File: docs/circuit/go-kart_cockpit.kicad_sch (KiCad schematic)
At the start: 28 parts, among them P1 Power, Q1 TIP120, SW1 SW_MEC_5E, X1 AVR-ISP-10, X10 Bluetooth-Modul, X11 Start/Stop/Rückwärts, X12 Taster rechts (male), X13 Taster links (male), X2 Display (2x3 male), X3 5V, X4 GND, X5 SDA, X6 24V Hupe, X7 J5, X8 J3, X9 SCL

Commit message: feat: first sketch of PCB
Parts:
- removed JP1: ~, Library:Bridge, symbol Jumper:Jumper_2_Bridged
- added JP10: Display_Vcc, Resistor_THT:R_Axial_DIN0207_L6.3mm_D2.5mm_P7.62mm_Horizontal, symbol Jumper:Jumper_2_Bridged
- added JP11: GND, Resistor_THT:R_Axial_DIN0207_L6.3mm_D2.5mm_P7.62mm_Horizontal, symbol Jumper:Jumper_2_Bridged
- added JP12: Display_Vcc, Resistor_THT:R_Axial_DIN0207_L6.3mm_D2.5mm_P15.24mm_Horizontal, symbol Jumper:Jumper_2_Bridged
- added JP2: GND, Resistor_THT:R_Axial_DIN0207_L6.3mm_D2.5mm_P15.24mm_Horizontal, symbol Jumper:Jumper_2_Bridged
- added JP3: ISP_SCK, Resistor_THT:R_Axial_DIN0207_L6.3mm_D2.5mm_P10.16mm_Horizontal, symbol Jumper:Jumper_2_Bridged
- added JP4: ISP_MOSI, Resistor_THT:R_Axial_DIN0207_L6.3mm_D2.5mm_P15.24mm_Horizontal, symbol Jumper:Jumper_2_Bridged
- added JP5: TXD0, Resistor_THT:R_Axial_DIN0207_L6.3mm_D2.5mm_P10.16mm_Horizontal, symbol Jumper:Jumper_2_Bridged
- added JP6: RXD0, Resistor_THT:R_Axial_DIN0207_L6.3mm_D2.5mm_P10.16mm_Horizontal, symbol Jumper:Jumper_2_Bridged
- added JP8: GND, Resistor_THT:R_Axial_DIN0207_L6.3mm_D2.5mm_P10.16mm_Horizontal, symbol Jumper:Jumper_2_Bridged
- added JP9: ~, Resistor_THT:R_Axial_DIN0207_L6.3mm_D2.5mm_P15.24mm_Horizontal, symbol Jumper:Jumper_2_Bridged
- P1: footprint LED_THT:LED_D5.0mm_Horizontal_O3.81mm_Z15.0mm -> LED_THT:LED_D3.0mm_Horizontal_O1.27mm_Z6.0mm
- Q1: footprint Package_TO_SOT_THT:TO-220-3_Horizontal_TabDown -> Library:TO-220-3_Horizontal_TabDown_no_hole
- R4: footprint Resistor_THT:R_Axial_DIN0204_L3.6mm_D1.6mm_P7.62mm_Horizontal -> Resistor_THT:R_Axial_DIN0309_L9.0mm_D3.2mm_P25.40mm_Horizontal
- R5: footprint Resistor_THT:R_Axial_DIN0204_L3.6mm_D1.6mm_P7.62mm_Horizontal -> Resistor_THT:R_Axial_DIN0207_L6.3mm_D2.5mm_P15.24mm_Horizontal
- R6: footprint Resistor_THT:R_Axial_DIN0204_L3.6mm_D1.6mm_P7.62mm_Horizontal -> Resistor_THT:R_Axial_DIN0207_L6.3mm_D2.5mm_P10.16mm_Horizontal
- X10: footprint Connector_JST:JST_EH_S4B-EH_1x04_P2.50mm_Horizontal -> Connector_PinSocket_2.54mm:PinSocket_1x04_P2.54mm_Horizontal
- X11, X6: footprint Library:Elecbee_3pin_Green_Connector_1.5mm -> Connector_Phoenix_MC_HighVoltage:PhoenixContact_MC_1,5_3-G-5.08_1x03_P5.08mm_Horizontal
- X2: value Display (2x3 male) -> Display (male)
- X3, X4, X5, X9: footprint Connector_PinHeader_2.54mm:PinHeader_1x01_P2.54mm_Vertical -> Connector_PinSocket_2.54mm:PinSocket_1x01_P2.54mm_Vertical
- X7, X8: footprint Connector_PinHeader_2.54mm:PinHeader_2x13_P2.54mm_Vertical -> Connector_PinSocket_2.54mm:PinSocket_2x13_P2.54mm_Vertical
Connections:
- net +24V: now also X6.3 (Pin_3); no longer X6.2 (Pin_2)
- net GND: now also X10.3 (Pin_3), JP11.1 (A), JP11.2 (B), JP2.1 (A), JP2.2 (B), JP8.1 (A), JP8.2 (B); no longer X10.2 (Pin_2)
- net PB1_SCK: now also X8.17 (Pin_17), JP3.1 (A); no longer X1.7 (SCK), X8.18 (Pin_18)
- net PB2_MOSI: now also X8.16 (Pin_16), JP4.1 (A); no longer X1.1 (MOSI), X8.15 (Pin_15)
- net PB3_MISO: now also X8.15 (Pin_15); no longer X8.16 (Pin_16)
- net PB4_OC2A: now also X8.14 (Pin_14); no longer X8.13 (Pin_13)
- net PC0_SW_BlinkerR: now also X7.24 (Pin_24); no longer X7.23 (Pin_23)
- net PC3_LED_BlinkerR: now also X7.26 (Pin_26); no longer X7.25 (Pin_25)
- net PD0_SCL: now also X7.14 (Pin_14); no longer X7.13 (Pin_13)
- net PD1_SDA: now also X7.13 (Pin_13); no longer X7.14 (Pin_14)
- net PD2_RXD1: now also X10.2 (Pin_2), X7.16 (Pin_16), JP9.1 (A), JP9.2 (B); no longer X10.3 (Pin_3)
- net PD3_TXD1: now also X7.15 (Pin_15); no longer X7.16 (Pin_16)
- net PD4_LED_GearUp: now also X7.18 (Pin_18); no longer X7.17 (Pin_17)
- net PE0_RXD0: now also X8.26 (Pin_26), JP6.1 (A); no longer X2.6 (Pin_6), X8.25 (Pin_25)
- net PE1_TXD0: now also X8.25 (Pin_25), JP5.1 (A); no longer X2.2 (Pin_2), X8.26 (Pin_26)
- net PE2_LED_BlinkerL: now also X8.24 (Pin_24); no longer X8.23 (Pin_23)
- net PE3_SW_BlinkerL: now also X8.23 (Pin_23); no longer X8.24 (Pin_24)
- net PE4_LED_LightSwitch: now also X8.22 (Pin_22); no longer X8.21 (Pin_21)
- net PE5_SW_LightSwitch: now also X8.21 (Pin_21); no longer X8.22 (Pin_22)
- net PE6_LED_Warnblinker: now also X8.20 (Pin_20); no longer X8.19 (Pin_19)
- net PE7_SW_Warnblinker: now also X8.19 (Pin_19); no longer X8.20 (Pin_20)
- net PG0_SW_GearUp: now also X7.20 (Pin_20); no longer X7.19 (Pin_19)
- net PG2_SW_GearDown: now also X7.22 (Pin_22); no longer X7.21 (Pin_21)
- net PG3_LED_GearDown: now also X7.12 (Pin_12); no longer X7.11 (Pin_11)
- net Vcc (5V): now also X10.4 (Pin_4), JP10.1 (A), JP10.2 (B), JP12.1 (A), JP12.2 (B); no longer X10.1 (Pin_1)
- net /PC2_SW_Start: now also X7.23 (Pin_23); no longer X7.24 (Pin_24)
- net /PG1_SW_Reverse: now also X7.19 (Pin_19); no longer X7.20 (Pin_20)
- net /RESET: now also X7.25 (Pin_25); no longer X7.26 (Pin_26)
- net at R5.2, R6.1: now also X10.1 (Pin_1); no longer X10.4 (Pin_4)
- net at Q1.2 (C), R3.2 (A): now also X6.2 (Pin_2); no longer X6.3 (Pin_3)
- net at R7.2: now also X11.1; no longer X11.3 (4)
- net at R8.2: now also X11.3 (4); no longer X11.1
- new net: JP5.2 (B), X2.2 (Pin_2)
- new net: JP6.2 (B), X2.6 (Pin_6)
- new net: JP4.2 (B), X1.1 (MOSI)
- new net: JP3.2 (B), X1.7 (SCK)
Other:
- moved on the sheet: R1, R7, R8, X1, X2, X5, X6, X7, X8, X9

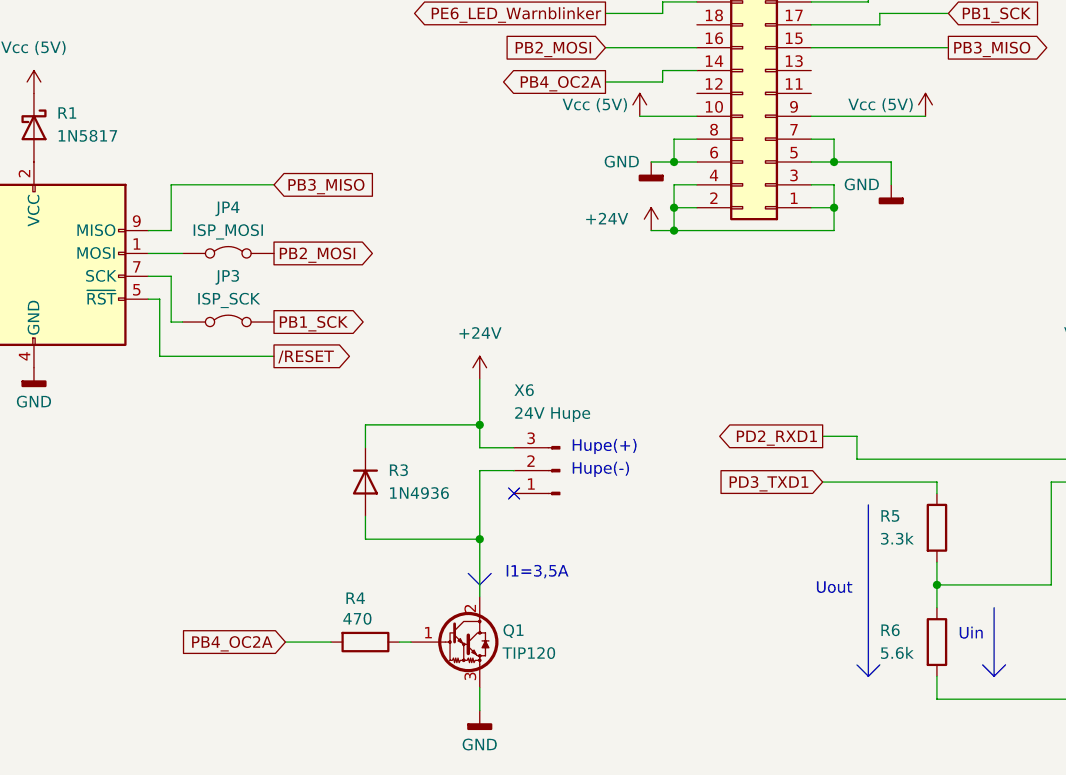
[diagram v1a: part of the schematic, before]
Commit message: feat(circuit): fixed DRC
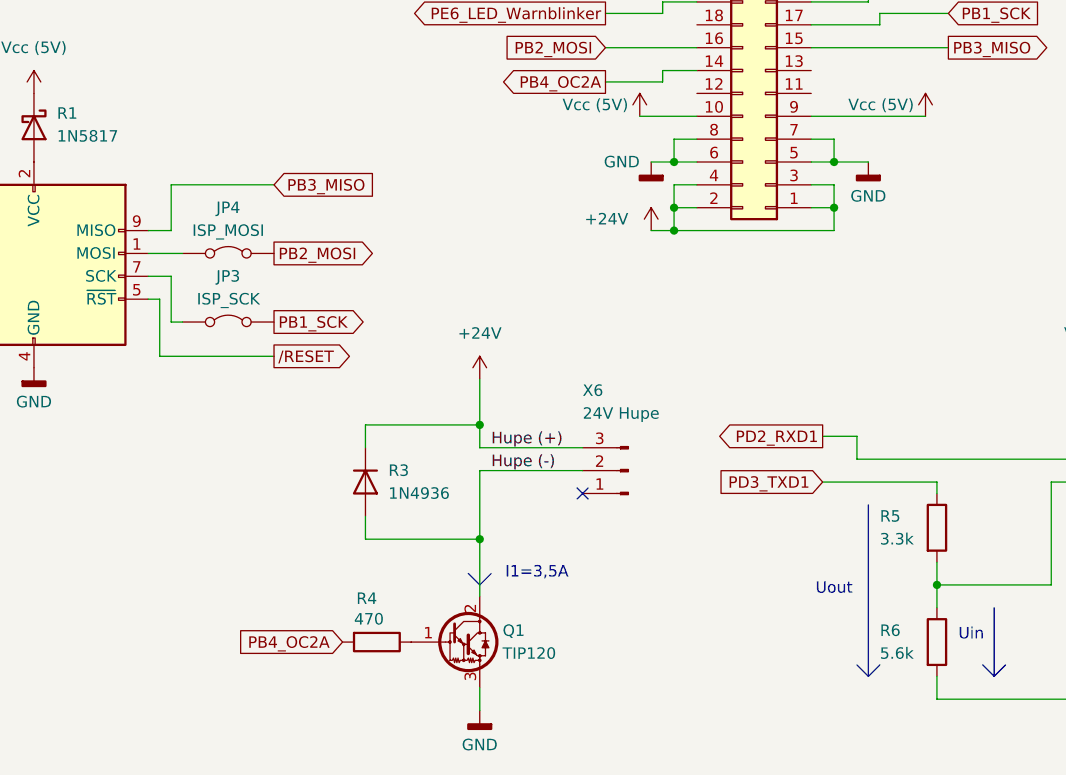
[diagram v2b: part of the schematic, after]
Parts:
- R2, R7, R8: footprint Resistor_THT:R_Axial_DIN0204_L3.6mm_D1.6mm_P7.62mm_Horizontal -> Resistor_THT:R_Axial_DIN0207_L6.3mm_D2.5mm_P10.16mm_Horizontal
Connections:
- net Hupe (-): now reaches Q1.2 (C), R3.2 (A), X6.2 (Pin_2)
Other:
- note removed: "Hupe(+)"
- note removed: "Hupe(-)"
- moved on the sheet: R4, X6

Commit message: feat(circuit): final touches
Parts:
- removed JP10: Display_Vcc, Resistor_THT:R_Axial_DIN0207_L6.3mm_D2.5mm_P7.62mm_Horizontal, symbol Jumper:Jumper_2_Bridged
- removed JP12: Display_Vcc, Resistor_THT:R_Axial_DIN0207_L6.3mm_D2.5mm_P15.24mm_Horizontal, symbol Jumper:Jumper_2_Bridged
- removed JP3: ISP_SCK, Resistor_THT:R_Axial_DIN0207_L6.3mm_D2.5mm_P10.16mm_Horizontal, symbol Jumper:Jumper_2_Bridged
- removed JP4: ISP_MOSI, Resistor_THT:R_Axial_DIN0207_L6.3mm_D2.5mm_P15.24mm_Horizontal, symbol Jumper:Jumper_2_Bridged
- removed JP5: TXD0, Resistor_THT:R_Axial_DIN0207_L6.3mm_D2.5mm_P10.16mm_Horizontal, symbol Jumper:Jumper_2_Bridged
- removed JP6: RXD0, Resistor_THT:R_Axial_DIN0207_L6.3mm_D2.5mm_P10.16mm_Horizontal, symbol Jumper:Jumper_2_Bridged
- removed JP9: ~, Resistor_THT:R_Axial_DIN0207_L6.3mm_D2.5mm_P15.24mm_Horizontal, symbol Jumper:Jumper_2_Bridged
- added X12: PD7, Connector_PinSocket_2.54mm:PinSocket_1x01_P2.54mm_Vertical, symbol Connector:Conn_01x01_Socket
- added X14: PG4, Connector_PinSocket_2.54mm:PinSocket_1x01_P2.54mm_Vertical, symbol Connector:Conn_01x01_Socket
- added X6: CS, Connector_PinSocket_2.54mm:PinSocket_1x01_P2.54mm_Vertical, symbol Connector:Conn_01x01_Socket
- added X7: PB6, Connector_PinSocket_2.54mm:PinSocket_1x01_P2.54mm_Vertical, symbol Connector:Conn_01x01_Socket
- added XB10: ISP_SCK, Resistor_THT:R_Axial_DIN0207_L6.3mm_D2.5mm_P10.16mm_Horizontal, symbol Jumper:Jumper_2_Bridged
- added XB2: ~, Resistor_THT:R_Axial_DIN0207_L6.3mm_D2.5mm_P15.24mm_Horizontal, symbol Jumper:Jumper_2_Bridged
- added XB3: Display_Vcc, Resistor_THT:R_Axial_DIN0207_L6.3mm_D2.5mm_P7.62mm_Horizontal, symbol Jumper:Jumper_2_Bridged
- added XB5: Display_Vcc, Resistor_THT:R_Axial_DIN0207_L6.3mm_D2.5mm_P15.24mm_Horizontal, symbol Jumper:Jumper_2_Bridged
- added XB6: TXD0, Resistor_THT:R_Axial_DIN0207_L6.3mm_D2.5mm_P10.16mm_Horizontal, symbol Jumper:Jumper_2_Bridged
- added XB7: RXD0, Resistor_THT:R_Axial_DIN0207_L6.3mm_D2.5mm_P10.16mm_Horizontal, symbol Jumper:Jumper_2_Bridged
- added XB9: ISP_MOSI, Resistor_THT:R_Axial_DIN0207_L6.3mm_D2.5mm_P15.24mm_Horizontal, symbol Jumper:Jumper_2_Bridged
- XB4: renamed from JP8; value GND -> Display_GND
- renumbered R2 to R1, R7 to R10, R9 to R2, R10 to R3, R3 to R4, R4 to R5, R5 to R6, R6 to R7, R1 to R8, R8 to R9, X12 to X1, X2 to X11, X5 to X13, X1 to X15, X13 to X16, X11 to X17, X3 to X2, X4 to X3, X6 to X4, X9 to X5, X7 to X8, X8 to X9, JP11 to XB1, JP2 to XB8
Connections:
- net GND: now also R1.2; no longer P1.1 (K)
- net PB1_SCK: now also X15.7 (SCK), XB10.1 (A), XB10.2 (B)
- net PB2_MOSI: now also X15.1 (MOSI), XB9.1 (A), XB9.2 (B)
- net PD2_RXD1: now also XB2.1 (A), XB2.2 (B)
- net PE0_RXD0: now also X11.6 (Pin_6), XB7.1 (A), XB7.2 (B)
- net PE1_TXD0: now also X11.2 (Pin_2), XB6.1 (A), XB6.2 (B)
- net Vcc (5V): now also P1.2 (A), XB3.1 (A), XB3.2 (B), XB5.1 (A), XB5.2 (B); no longer R1.1
- net BL_RX3V3: now reaches R6.2, R7.1, X10.1 (Pin_1)
- net PG4: now reaches X8.11 (Pin_11)
- net PG4: now also X14.1 (Pin_1)
- net PD7: now reaches X8.17 (Pin_17)
- net PD7: now also X12.1 (Pin_1)
- net PB6_OC1B: now reaches X9.12 (Pin_12)
- net PB6_OC1B: now also X7.1 (Pin_1)
- net PB0_CS: now reaches X9.18 (Pin_18)
- net PB0_CS: now also X6.1 (Pin_1)
- new net: P1.1 (K), R1.1
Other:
- note added: "Alle Widerstände aus der E12-Reihe mit 10% Toleranz. Das Slash (/) wird als Indikation für negativ Logik genutzt. Für /PG1_SW_Reverse und /PC2_SW_Start müssen die Pull-Up-Widerstände des AT90CAN32 Mikrocontrollers aktiviert werden."
- note removed: "Das Slash (/) wird als indikation für negativ Logik genutzt. Alle Taster und Wechsler agieren als Pull-Down. Das heißt die Pull-Up-Widerstände des AT90CAN32 Mikrocontrollers müssen aktiviert werden. Alle Widerstände aus der E12-Reihe mit 10% Toleranz."
- title: go-kart_cockpit -> JCS-BK1091_GO-KART_Cockpitplatine
- moved on the sheet: P1, Q1, R1, R10, R4, R5, R6, R7, R8, R9, X1, X10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
